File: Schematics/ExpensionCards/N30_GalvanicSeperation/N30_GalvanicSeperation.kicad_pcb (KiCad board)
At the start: 2 copper layers, 95.8 x 62.8 mm, 45 parts, among them X3010 Conn_01x01_MountingPin, X3011 Conn_01x01_MountingPin, X3012 Conn_01x01_MountingPin

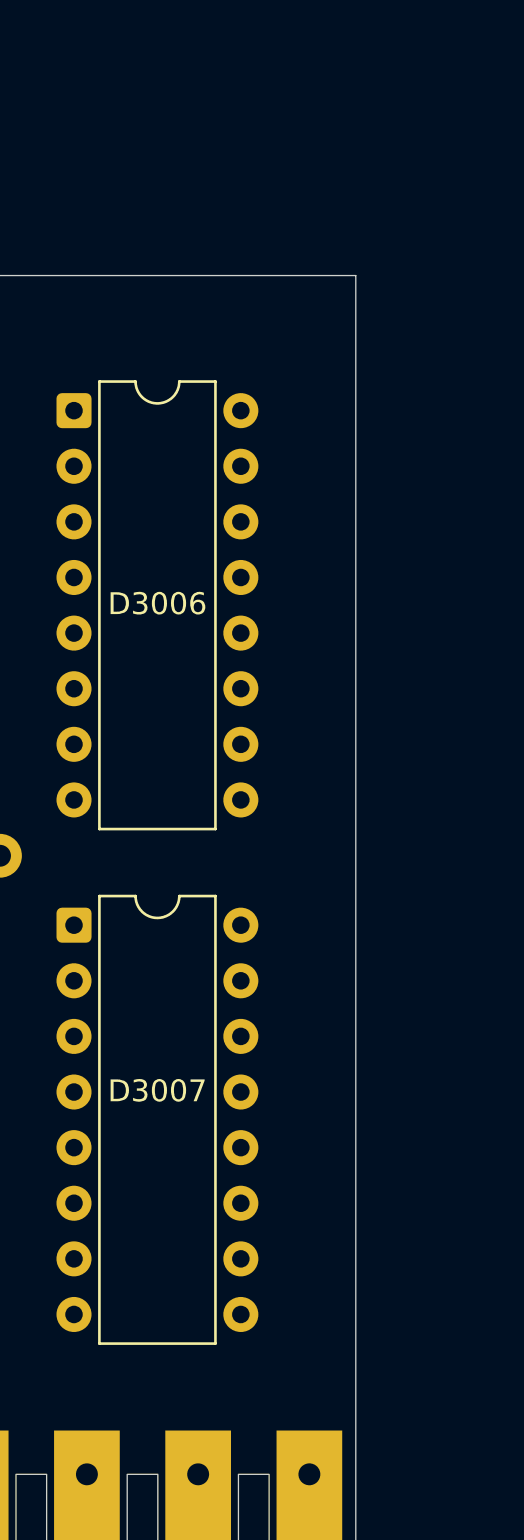
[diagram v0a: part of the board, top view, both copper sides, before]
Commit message: Updated disassembly some more Moved PM2528 footprints/3D to subfolder
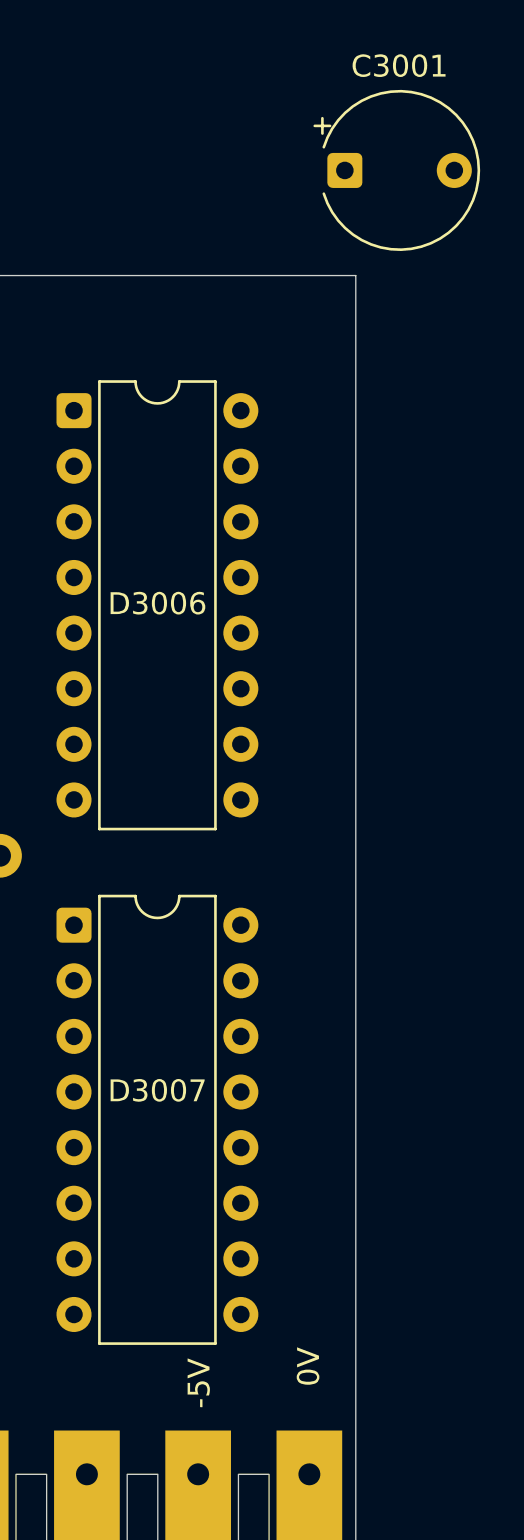
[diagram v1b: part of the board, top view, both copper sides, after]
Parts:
- added C3001: 33u, Capacitor_THT:CP_Radial_Tantal_D7.0mm_P5.00mm, F.Cu at (200.8, 67.0)
- X3001: footprint PM2528:PM2528_RiserCardConnector -> Philips_PM2528:PM2528_RiserCardConnector
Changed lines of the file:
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@@
 		)
 	)
+	(footprint "Capacitor_THT:CP_Radial_Tantal_D7.0mm_P5.00mm"
+		(layer "F.Cu")
+		(at 200.75 67)
+		(descr "CP, Radial_Tantal series, Radial, pin pitch=5.00mm, diameter=7.0mm, height=10mm, Tantal Electrolytic Capacitor, http://cdn-reichelt.de/documents/datenblatt/B300/TANTAL-TB-Serie%23.pdf")
+		(tags "CP Radial_Tantal series Radial pin pitch 5.00mm diameter 7.0mm height 10mm Tantal Electrolytic Capacitor")
+		(property "Reference" "C3001"
+			(at 2.5 -4.75 0)
+			(layer "F.SilkS")
+			(effects
+				(font
+					(size 1 1)
+					(thickness 0.15)
+				)
+			)
+		)
+		(property "Value" "33u"
+			(at 2.5 4.75 0)
+			(layer "F.Fab")
+			(effects
+				(font
+					(size 1 1)
+					(thickness 0.15)
+				)
+			)
+		)
+		(property "Datasheet" "~"
+			(at 0 0 0)
+			(layer "F.Fab")
+			(hide yes)
+			(effects
+				(font
+					(size 1.27 1.27)
+					(thickness 0.15)
+				)
+			)
+		)
+		(property "Description" "Polarized capacitor"
+			(at 0 0 0)
+			(layer "F.Fab")
+			(hide yes)
+			(effects
+				(font
+					(size 1.27 1.27)
+					(thickness 0.15)
+				)
+			)
+		)
+		(property ki_fp_filters "CP_*")
+		(sheetname "/")
+		(sheetfile "N30_GalvanicSeperation.kicad_sch")
+		(attr through_hole)
+		(fp_line
+			(start -1.374723 -2.035)
+			(end -0.674723 -2.035)
+			(stroke
+				(width 0.12)
+				(type solid)
+			)
+			(layer "F.SilkS")
+		)
+		(fp_line
+			(start -1.024723 -2.385)
+			(end -1.024723 -1.685)
+			(stroke
+				(width 0.12)
+				(type solid)
+			)
+			(layer "F.SilkS")
+		)
+		(fp_arc
+			(start -0.961329 -1.06)
+			(mid 6.12 0)
+			(end -0.961329 1.06)
+			(stroke
+				(width 0.12)
+				(type solid)
+			)
+			(layer "F.SilkS")
+		)
+		(fp_circle
+			(center 2.5 0)
+			(end 6.25 0)
+			(stroke
+				(width 0.05)
+				(type solid)
+			)
+			(fill no)
+			(layer "F.CrtYd")
+		)
+		(fp_line
+			(start -0.495708 -1.5275)
+			(end 0.204292 -1.5275)
+			(stroke
+				(width 0.1)
+				(type solid)
+			)
+			(layer "F.Fab")
+		)
+		(fp_line
+			(start -0.145708 -1.8775)
+			(end -0.145708 -1.1775)
+			(stroke
+				(width 0.1)
+				(type solid)
+			)
+			(layer "F.Fab")
+		)
+		(fp_circle
+			(center 2.5 0)
+			(end 6 0)
+			(stroke
+				(width 0.1)
+				(type solid)
+			)
+			(fill no)
+			(layer "F.Fab")
+		)
+		(fp_text user "${REFERENCE}"
+			(at 2.5 0 0)
+			(layer "F.Fab")
+			(effects
+				(font
+					(size 1 1)
+					(thickness 0.15)
+				)
+			)
+		)
+		(pad "1" thru_hole roundrect
+			(at 0 0)
+			(size 1.6 1.6)
+			(drill 0.8)
+			(layers "*.Cu" "*.Mask")
+			(remove_unused_layers no)
+			(roundrect_rratio 0.15625)
+			(net 1 "GND2")
+			(pintype "passive")
+		)
+		(pad "2" thru_hole circle
+			(at 5 0)
+			(size 1.6 1.6)
+			(drill 0.8)
+			(layers "*.Cu" "*.Mask")
+			(remove_unused_layers no)
+			(net 19 "-5V")
+			(pintype "passive")
+		)
+		(embedded_fonts no)
+		(model "${KICAD9_3DMODEL_DIR}/Capacitor_THT.3dshapes/CP_Radial_Tantal_D7.0mm_P5.00mm.step"
+			(offset
+				(xyz 0 0 0)
+			)
+			(scale
+				(xyz 1 1 1)
+			)
+			(rotate
+				(xyz 0 0 0)
+			)
+		)
+	)
 	(footprint "Capacitor_THT:C_Axial_L5.1mm_D3.1mm_P10.00mm_Horizontal"
 		(layer "F.Cu")
@@
 		)
 	)
-	(footprint "PM2528:PM2528_RiserCardConnector"
+	(footprint "Philips_PM2528:PM2528_RiserCardConnector"
 		(layer "F.Cu")
 		(at 107.69 126.55 90)
 		(property "Reference" "X3001"
-			(at 0 -0.5 90)
+			(at -7 -4.5 90)
 			(unlocked yes)
 			(layer "F.SilkS")
@@
 		)
 		(property "Value" "~"
-			(at 0 1 90)
+			(at -0.5 -3 90)
 			(unlocked yes)
 			(layer "F.Fab")
@@
 			(layer "F.CrtYd")
 		)
+		(fp_text user "-5V"
+			(at 3 87 90)
+			(unlocked yes)
+			(layer "F.SilkS")
+			(effects
+				(font
+					(size 1 1)
+					(thickness 0.1)
+				)
+				(justify left bottom)
+			)
+		)
+		(fp_text user "0V"
+			(at 4 92 90)
+			(unlocked yes)
+			(layer "F.SilkS")
+			(effects
+				(font
+					(size 1 1)
+					(thickness 0.1)
+				)
+				(justify left bottom)
+			)
+		)
 		(fp_text user "${REFERENCE}"
-			(at 0 2.5 90)
+			(at 5 -4.5 90)
 			(unlocked yes)
 			(layer "F.Fab")
